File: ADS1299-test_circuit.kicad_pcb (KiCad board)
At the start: 2 copper layers, 90.4 x 96.4 mm, 111 parts, among them J1 OUT, J2 GND, J3 GND, P1 +5V, P10 IN2, P11 IN6, P12 IN5, P13 IN1, P14 BiasOut_C, P15 BiasOut_R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

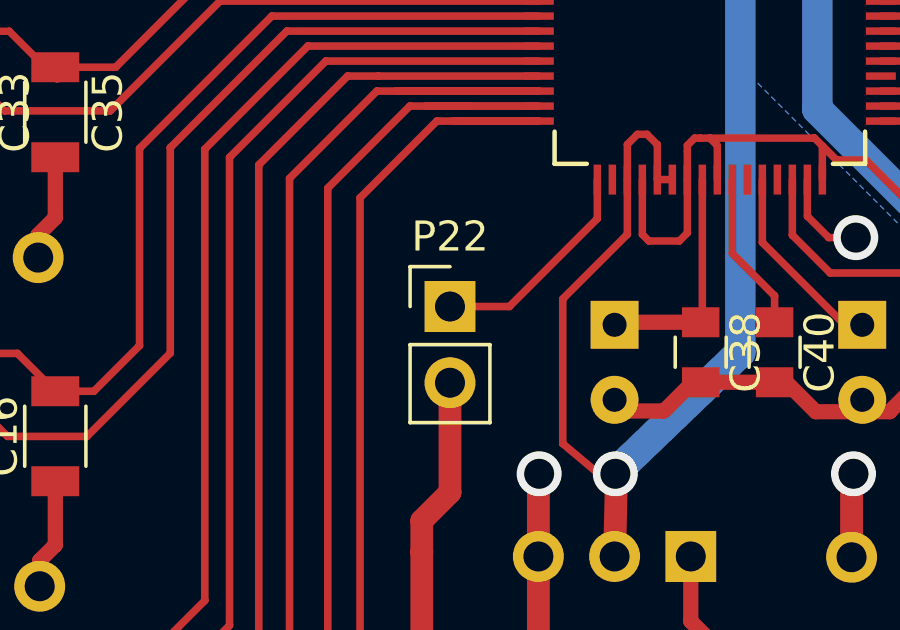
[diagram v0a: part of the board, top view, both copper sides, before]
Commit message: Correccion de pines, masa, capacitores.
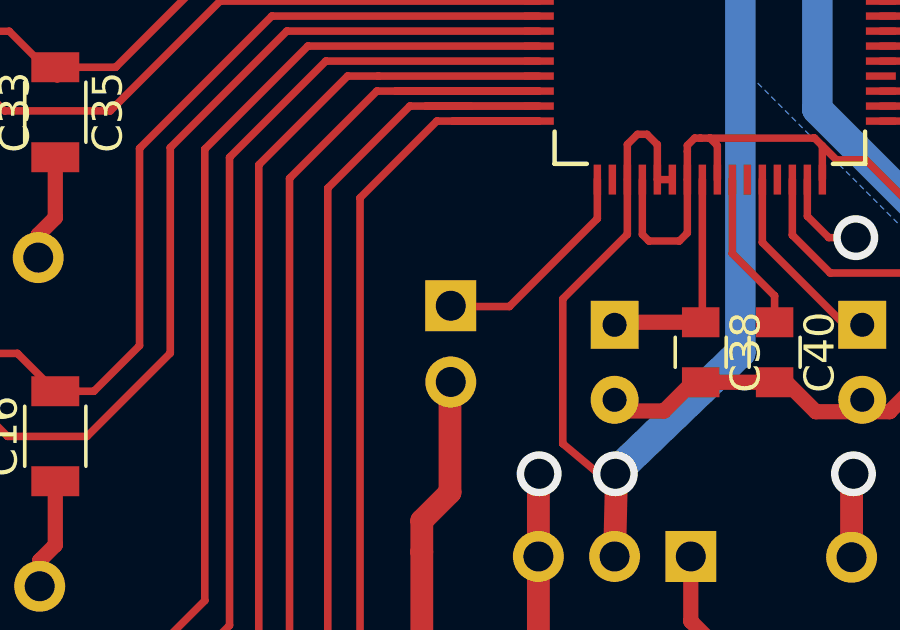
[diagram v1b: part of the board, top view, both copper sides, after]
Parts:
- P22: moved to B.Cu
- turned P22 to 180 degrees
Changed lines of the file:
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@@
     )
   )
-  (module Pin_Headers:Pin_Header_Straight_1x02_Pitch2.54mm (layer F.Cu)
-    (at 157.0736 72.7964)
+  (module Pin_Headers:Pin_Header_Straight_1x02_Pitch2.54mm (layer B.Cu)
+    (at 157.099 72.771 180)
     (descr "Through hole straight pin header, 1x02, 2.54mm pitch, single row")
     (tags "Through hole pin header THT 1x02 2.54mm single row")
-    (fp_text reference P22 (at 0 -2.33) (layer F.SilkS)
-      (effects (font (size 1 1) (thickness 0.15)))
+    (fp_text reference P22 (at 0 2.33 180) (layer B.SilkS)
+      (effects (font (size 1 1) (thickness 0.15)) (justify mirror))
     )
-    (fp_text value D/Ref (at 0 4.87) (layer F.Fab)
-      (effects (font (size 1 1) (thickness 0.15)))
+    (fp_text value D/Ref (at 0 -4.87 180) (layer B.Fab)
+      (effects (font (size 1 1) (thickness 0.15)) (justify mirror))
     )
-    (fp_line (start -1.27 -1.27) (end -1.27 3.81) (layer F.Fab) (width 0.1))
-    (fp_line (start -1.27 3.81) (end 1.27 3.81) (layer F.Fab) (width 0.1))
-    (fp_line (start 1.27 3.81) (end 1.27 -1.27) (layer F.Fab) (width 0.1))
-    (fp_line (start 1.27 -1.27) (end -1.27 -1.27) (layer F.Fab) (width 0.1))
-    (fp_line (start -1.33 1.27) (end -1.33 3.87) (layer F.SilkS) (width 0.12))
-    (fp_line (start -1.33 3.87) (end 1.33 3.87) (layer F.SilkS) (width 0.12))
-    (fp_line (start 1.33 3.87) (end 1.33 1.27) (layer F.SilkS) (width 0.12))
-    (fp_line (start 1.33 1.27) (end -1.33 1.27) (layer F.SilkS) (width 0.12))
-    (fp_line (start -1.33 0) (end -1.33 -1.33) (layer F.SilkS) (width 0.12))
-    (fp_line (start -1.33 -1.33) (end 0 -1.33) (layer F.SilkS) (width 0.12))
-    (fp_line (start -1.8 -1.8) (end -1.8 4.35) (layer F.CrtYd) (width 0.05))
-    (fp_line (start -1.8 4.35) (end 1.8 4.35) (layer F.CrtYd) (width 0.05))
-    (fp_line (start 1.8 4.35) (end 1.8 -1.8) (layer F.CrtYd) (width 0.05))
-    (fp_line (start 1.8 -1.8) (end -1.8 -1.8) (layer F.CrtYd) (width 0.05))
-    (fp_text user %R (at 0 -2.33) (layer F.Fab)
-      (effects (font (size 1 1) (thickness 0.15)))
+    (fp_line (start -1.27 1.27) (end -1.27 -3.81) (layer B.Fab) (width 0.1))
+    (fp_line (start -1.27 -3.81) (end 1.27 -3.81) (layer B.Fab) (width 0.1))
+    (fp_line (start 1.27 -3.81) (end 1.27 1.27) (layer B.Fab) (width 0.1))
+    (fp_line (start 1.27 1.27) (end -1.27 1.27) (layer B.Fab) (width 0.1))
+    (fp_line (start -1.33 -1.27) (end -1.33 -3.87) (layer B.SilkS) (width 0.12))
+    (fp_line (start -1.33 -3.87) (end 1.33 -3.87) (layer B.SilkS) (width 0.12))
+    (fp_line (start 1.33 -3.87) (end 1.33 -1.27) (layer B.SilkS) (width 0.12))
+    (fp_line (start 1.33 -1.27) (end -1.33 -1.27) (layer B.SilkS) (width 0.12))
+    (fp_line (start -1.33 0) (end -1.33 1.33) (layer B.SilkS) (width 0.12))
+    (fp_line (start -1.33 1.33) (end 0 1.33) (layer B.SilkS) (width 0.12))
+    (fp_line (start -1.8 1.8) (end -1.8 -4.35) (layer B.CrtYd) (width 0.05))
+    (fp_line (start -1.8 -4.35) (end 1.8 -4.35) (layer B.CrtYd) (width 0.05))
+    (fp_line (start 1.8 -4.35) (end 1.8 1.8) (layer B.CrtYd) (width 0.05))
+    (fp_line (start 1.8 1.8) (end -1.8 1.8) (layer B.CrtYd) (width 0.05))
+    (fp_text user %R (at 0 2.33 180) (layer B.Fab)
+      (effects (font (size 1 1) (thickness 0.15)) (justify mirror))
     )
-    (pad 1 thru_hole rect (at 0 0) (size 1.7 1.7) (drill 1) (layers *.Cu *.Mask)
+    (pad 1 thru_hole rect (at 0 0 180) (size 1.7 1.7) (drill 1) (layers *.Cu *.Mask)
       (net 107 "Net-(P22-Pad1)"))
-    (pad 2 thru_hole oval (at 0 2.54) (size 1.7 1.7) (drill 1) (layers *.Cu *.Mask)
+    (pad 2 thru_hole oval (at 0 -2.54 180) (size 1.7 1.7) (drill 1) (layers *.Cu *.Mask)
       (net 5 "Net-(C12-Pad2)"))
     (model ${KISYS3DMOD}/Pin_Headers.3dshapes/Pin_Header_Straight_1x02_Pitch2.54mm.wrl

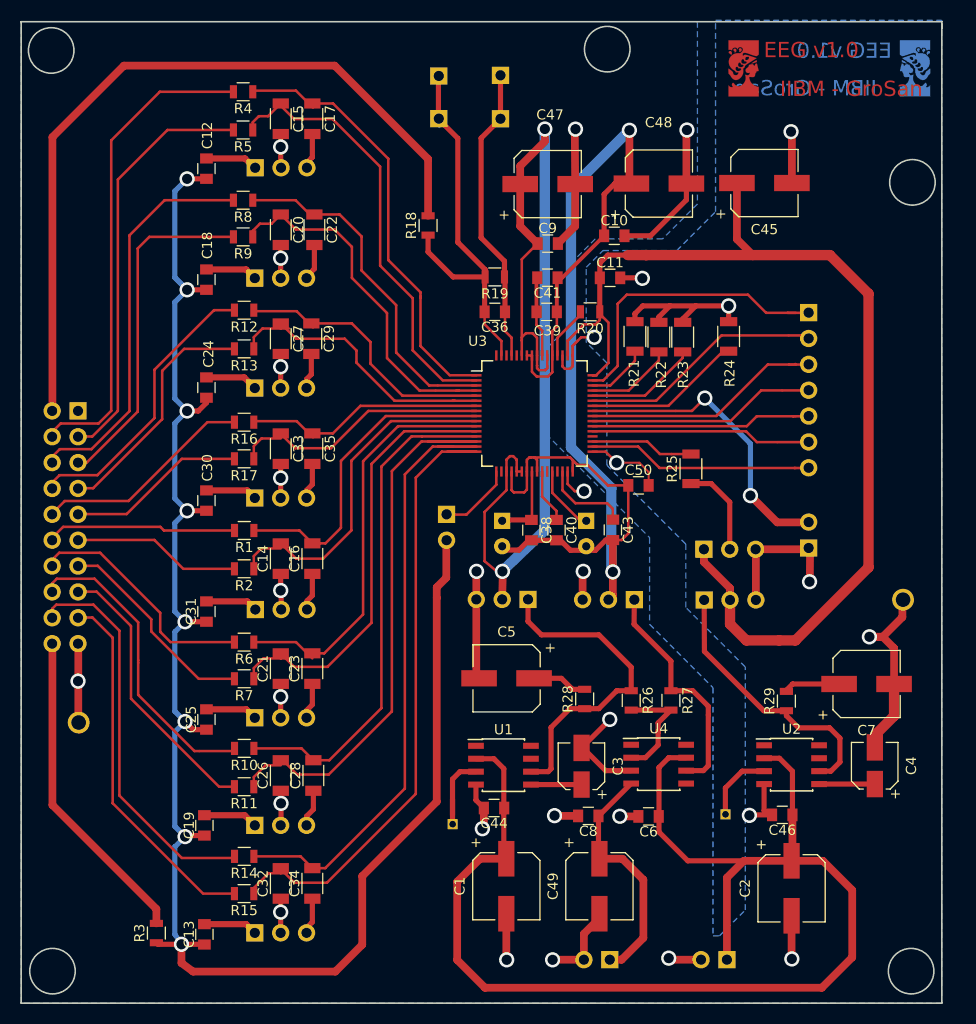
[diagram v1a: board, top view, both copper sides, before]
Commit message: Arreglos LCI
- Pistas mas gruesas donde es posible.
- Pines de TEMP se corrigieron a 2.57mm.
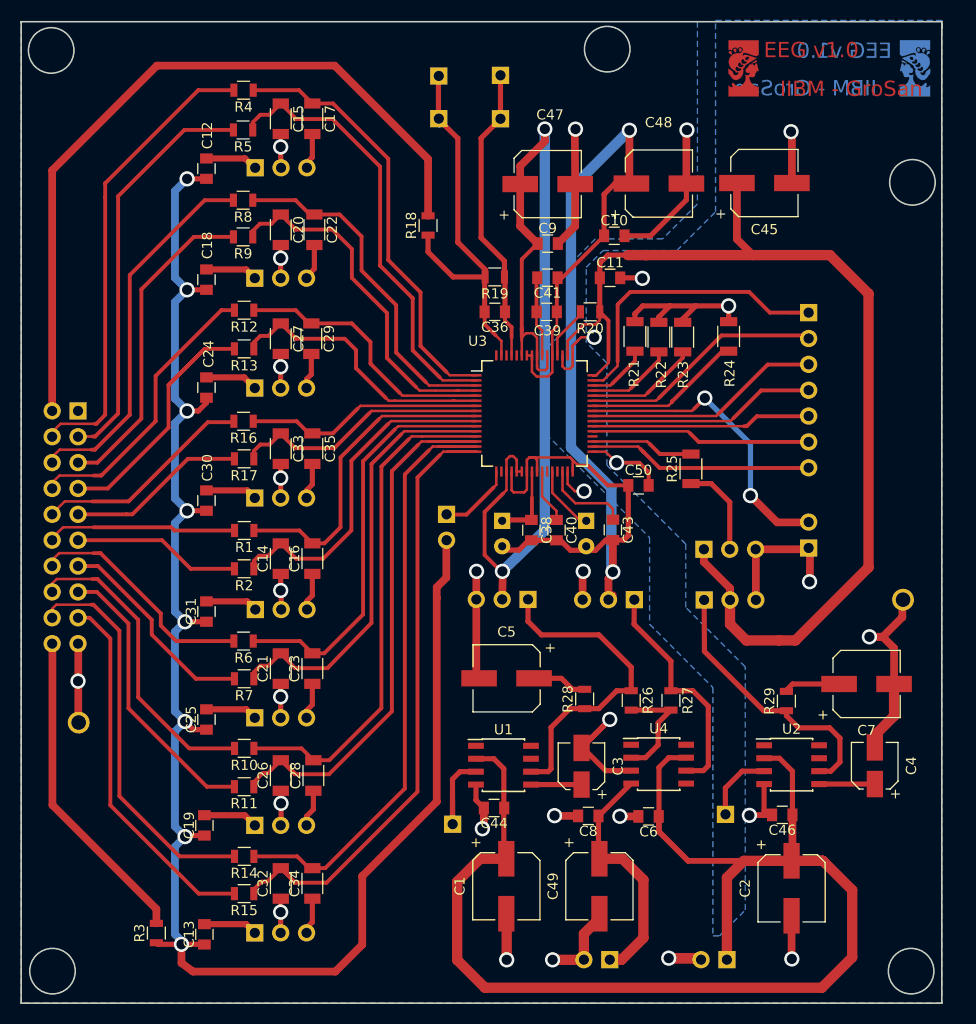
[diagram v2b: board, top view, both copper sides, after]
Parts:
- P18, P2: footprint Pin_Headers:Pin_Header_Straight_1x01_Pitch1.27mm -> Pin_Headers:Pin_Header_Straight_1x01_Pitch2.54mm
- moved R4 0.16 mm to (137.2, 31.1)
- moved R6 0.12 mm to (137.2, 85.2)
- moved R16 0.11 mm to (137.2, 63.6)
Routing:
- net +5: track 130.2 -> 216.9 mm
- net Net-(C12-Pad2): track 237.0 -> 310.2 mm
- net Net-(C32-Pad2): track 62.9 -> 111.5 mm
- net Net-(C34-Pad2): track 62.0 -> 105.2 mm
- net Net-(C26-Pad2): track 57.5 -> 95.0 mm
- net Net-(C28-Pad2): track 49.4 -> 86.6 mm
- net Net-(C17-Pad1): track 42.9 -> 71.9 mm
- net Net-(C15-Pad1): track 43.7 -> 69.8 mm
- net Net-(C22-Pad1): track 34.2 -> 59.1 mm
- net GND: track 199.9 -> 224.8 mm
- net Net-(C21-Pad2): track 43.4 -> 66.5 mm
- net Net-(C23-Pad2): track 40.6 -> 62.3 mm
- net Net-(C16-Pad2): track 32.2 -> 48.6 mm
- net Net-(C14-Pad2): track 33.7 -> 49.1 mm
- net Net-(C20-Pad1): track 35.1 -> 49.8 mm
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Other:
- net class Default: clearance 0.1 -> 0.21
- rule trace_clearance: 0.1 -> 0.21

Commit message: Correcciones LCI
Ahora las vias son pines con thermal relief.
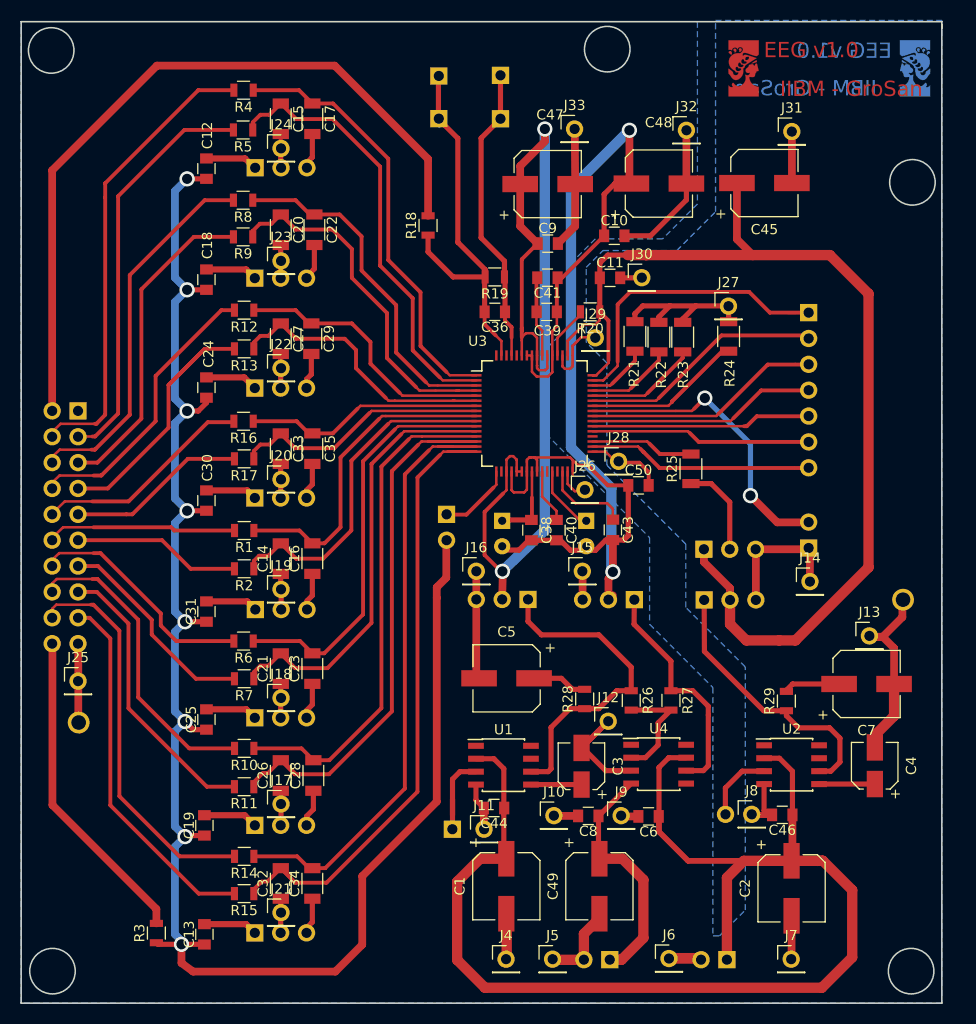
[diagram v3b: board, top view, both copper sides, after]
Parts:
- added J10: CONN_01X01, Pin_Headers:Pin_Header_Straight_1x01_Pitch2.54mm, F.Cu at (167.6, 102.4)
- added J11: CONN_01X01, Pin_Headers:Pin_Header_Straight_1x01_Pitch2.54mm, F.Cu at (160.8, 103.7)
- added J12: CONN_01X01, Pin_Headers:Pin_Header_Straight_1x01_Pitch2.54mm, F.Cu at (173.0, 93.1)
- added J13: CONN_01X01, Pin_Headers:Pin_Header_Straight_1x01_Pitch2.54mm, F.Cu at (198.6, 84.7)
- added J14: CONN_01X01, Pin_Headers:Pin_Header_Straight_1x01_Pitch2.54mm, F.Cu at (192.8, 79.4)
- added J15: CONN_01X01, Pin_Headers:Pin_Header_Straight_1x01_Pitch2.54mm, F.Cu at (170.4, 78.4)
- added J16: CONN_01X01, Pin_Headers:Pin_Header_Straight_1x01_Pitch2.54mm, F.Cu at (160.0, 78.4)
- added J17: CONN_01X01, Pin_Headers:Pin_Header_Straight_1x01_Pitch2.54mm, F.Cu at (140.8, 101.2)
- added J18: CONN_01X01, Pin_Headers:Pin_Header_Straight_1x01_Pitch2.54mm, F.Cu at (140.8, 90.8)
- added J19: CONN_01X01, Pin_Headers:Pin_Header_Straight_1x01_Pitch2.54mm, F.Cu at (140.8, 80.1)
- added J20: CONN_01X01, Pin_Headers:Pin_Header_Straight_1x01_Pitch2.54mm, F.Cu at (140.8, 69.3)
- added J21: CONN_01X01, Pin_Headers:Pin_Header_Straight_1x01_Pitch2.54mm, F.Cu at (140.8, 111.9)
- added J22: CONN_01X01, Pin_Headers:Pin_Header_Straight_1x01_Pitch2.54mm, F.Cu at (140.8, 58.4)
- added J23: CONN_01X01, Pin_Headers:Pin_Header_Straight_1x01_Pitch2.54mm, F.Cu at (140.8, 47.9)
- added J24: CONN_01X01, Pin_Headers:Pin_Header_Straight_1x01_Pitch2.54mm, F.Cu at (140.8, 36.8)
- added J25: CONN_01X01, Pin_Headers:Pin_Header_Straight_1x01_Pitch2.54mm, F.Cu at (120.9, 89.2)
- added J26: CONN_01X01, Pin_Headers:Pin_Header_Straight_1x01_Pitch2.54mm, F.Cu at (170.7, 70.4)
- added J27: CONN_01X01, Pin_Headers:Pin_Header_Straight_1x01_Pitch2.54mm, F.Cu at (184.8, 52.3)
- added J28: CONN_01X01, Pin_Headers:Pin_Header_Straight_1x01_Pitch2.54mm, F.Cu at (174.0, 67.6)
- added J29: CONN_01X01, Pin_Headers:Pin_Header_Straight_1x01_Pitch2.54mm, F.Cu at (171.7, 55.4)
- added J30: CONN_01X01, Pin_Headers:Pin_Header_Straight_1x01_Pitch2.54mm, F.Cu at (176.3, 49.5)
- added J31: CONN_01X01, Pin_Headers:Pin_Header_Straight_1x01_Pitch2.54mm, F.Cu at (191.0, 35.2)
- added J32: CONN_01X01, Pin_Headers:Pin_Header_Straight_1x01_Pitch2.54mm, F.Cu at (180.7, 35.1)
- added J33: CONN_01X01, Pin_Headers:Pin_Header_Straight_1x01_Pitch2.54mm, F.Cu at (169.7, 34.9)
- added J4: CONN_01X01, Pin_Headers:Pin_Header_Straight_1x01_Pitch2.54mm, F.Cu at (162.9, 116.5)
- added J5: CONN_01X01, Pin_Headers:Pin_Header_Straight_1x01_Pitch2.54mm, F.Cu at (167.5, 116.5)
- added J6: CONN_01X01, Pin_Headers:Pin_Header_Straight_1x01_Pitch2.54mm, F.Cu at (178.9, 116.4)
- added J7: CONN_01X01, Pin_Headers:Pin_Header_Straight_1x01_Pitch2.54mm, F.Cu at (190.9, 116.5)
- added J8: CONN_01X01, Pin_Headers:Pin_Header_Straight_1x01_Pitch2.54mm, F.Cu at (187.1, 102.2)
- added J9: CONN_01X01, Pin_Headers:Pin_Header_Straight_1x01_Pitch2.54mm, F.Cu at (174.2, 102.4)
- moved P2 0.50 mm to (157.7, 103.7)
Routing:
- net GND: vias 30 -> 0
